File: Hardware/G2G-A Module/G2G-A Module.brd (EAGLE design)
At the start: 13.1 x 12.8 mm, 4 parts, among them J1 GROVE-4P-2.0-3470130P1

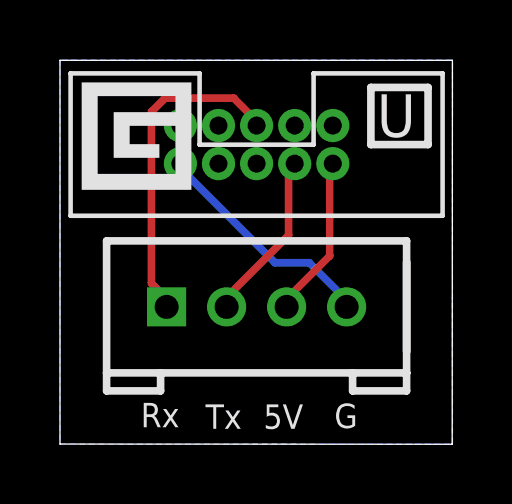
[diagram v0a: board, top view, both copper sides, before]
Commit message: Added G2G-A and G2G-I modules.
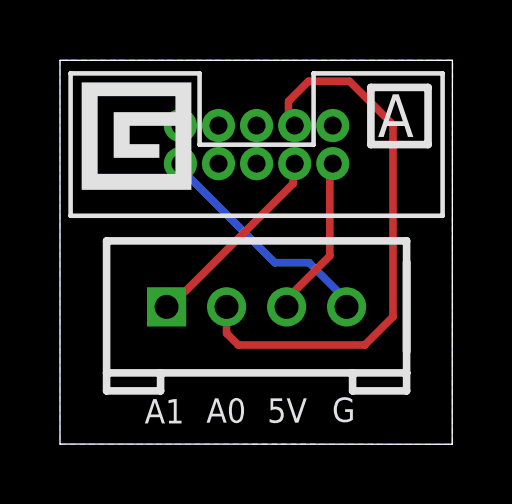
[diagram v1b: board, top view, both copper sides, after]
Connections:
- removed net RX: J1.1, U$1.5
- removed net TX: J1.2, U$1.4
- new net A0: J1.2, U$1.3
- new net A1: J1.1, U$1.4
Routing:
- net A0: track 0.00 -> 18.6 mm
- net RX: track 10.9 -> 0.00 mm
- net A1: track 0.00 -> 6.59 mm
- net TX: track 5.75 -> 0.00 mm
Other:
- board text added: "A"
- board text added: "A0"
- board text added: "A1"
- board text added: "G2G-A"
- board text removed: "G2G-U"
- board text removed: "Rx"
- board text removed: "Tx"
- board text removed: "U"
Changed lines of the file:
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@@
 <wire x1="13.0812" y1="12.7916" x2="0" y2="12.7916" width="0" layer="20"/>
 <wire x1="0" y1="12.7916" x2="0" y2="0" width="0" layer="20"/>
-<text x="10.5664" y="10.2362" size="1.4224" layer="21">U</text>
+<text x="10.5918" y="10.2362" size="1.4224" layer="21">A</text>
 <wire x1="10.3632" y1="11.8872" x2="10.3632" y2="9.9822" width="0.254" layer="21"/>
 <wire x1="10.3632" y1="9.9822" x2="12.2682" y2="9.9822" width="0.254" layer="21"/>
 <wire x1="12.2682" y1="9.9822" x2="12.2682" y2="11.8872" width="0.254" layer="21"/>
 <wire x1="12.2682" y1="11.8872" x2="10.3632" y2="11.8872" width="0.254" layer="21"/>
-<text x="12.5476" y="1.905" size="1.016" layer="22" rot="MR0">G2G-U</text>
+<text x="12.5222" y="1.905" size="1.016" layer="22" rot="MR0">G2G-A</text>
 <text x="12.5222" y="0.6096" size="1.016" layer="22" rot="MR0">v1.0</text>
-<text x="2.6924" y="0.5588" size="0.8128" layer="21">Rx</text>
-<text x="4.8514" y="0.508" size="0.8128" layer="21">Tx</text>
-<text x="6.7818" y="0.508" size="0.8128" layer="21">5V</text>
-<text x="9.144" y="0.5334" size="0.8128" layer="21">G</text>
-<text x="12.5984" y="5.7912" size="1.4224" layer="22" rot="MR0">Gadgeteer.in'</text>
+<text x="6.9088" y="0.7112" size="0.8128" layer="21">5V</text>
+<text x="9.0678" y="0.7366" size="0.8128" layer="21">G</text>
+<text x="12.6238" y="5.7658" size="1.4224" layer="22" rot="MR0">Gadgeteer.in'</text>
 <rectangle x1="0.7225" y1="8.4731" x2="4.3801" y2="8.5493" layer="21"/>
 <rectangle x1="0.7225" y1="8.5493" x2="4.3801" y2="8.6255" layer="21"/>
@@
 <rectangle x1="0.7225" y1="11.9021" x2="4.3801" y2="11.9783" layer="21"/>
 <rectangle x1="0.7225" y1="11.9783" x2="4.3801" y2="12.0545" layer="21"/>
+<text x="4.8768" y="0.7112" size="0.8128" layer="21">A0</text>
+<text x="2.8194" y="0.6858" size="0.8128" layer="21">A1</text>
 </plain>
 <attributes>
@@
 </elements>
 <signals>
-<signal name="TX">
-<contactref element="U$1" pad="4"/>
-<contactref element="J1" pad="2"/>
-<wire x1="7.62" y1="6.9596" x2="7.62" y2="9.2456" width="0.254" layer="1"/>
-<wire x1="5.5626" y1="4.9022" x2="7.62" y2="6.9596" width="0.254" layer="1"/>
-<wire x1="7.62" y1="9.2456" x2="7.8232" y2="9.3472" width="0.254" layer="1"/>
-<wire x1="5.5626" y1="4.9022" x2="5.5532" y2="4.572" width="0.254" layer="1"/>
-</signal>
-<signal name="RX">
-<contactref element="U$1" pad="5"/>
-<contactref element="J1" pad="1"/>
-<wire x1="6.477" y1="10.8458" x2="6.477" y2="10.6172" width="0.254" layer="1"/>
-<wire x1="5.7912" y1="11.5316" x2="6.477" y2="10.8458" width="0.254" layer="1"/>
-<wire x1="3.5052" y1="11.5316" x2="5.7912" y2="11.5316" width="0.254" layer="1"/>
-<wire x1="3.048" y1="11.0744" x2="3.5052" y2="11.5316" width="0.254" layer="1"/>
-<wire x1="3.048" y1="5.3594" x2="3.048" y2="11.0744" width="0.254" layer="1"/>
-<wire x1="3.5052" y1="4.9022" x2="3.048" y2="5.3594" width="0.254" layer="1"/>
-<wire x1="6.477" y1="10.6172" x2="6.5532" y2="10.6172" width="0.254" layer="1"/>
-<wire x1="3.5052" y1="4.9022" x2="3.5532" y2="4.572" width="0.254" layer="1"/>
-</signal>
 <signal name="GND">
 <contactref element="U$1" pad="10"/>
@@
 <wire x1="7.62" y1="4.9022" x2="7.5532" y2="4.572" width="0.254" layer="1"/>
 </signal>
+<signal name="A0">
+<contactref element="J1" pad="2"/>
+<contactref element="U$1" pad="3"/>
+<wire x1="5.5532" y1="4.572" x2="5.5532" y2="3.6924" width="0.254" layer="1"/>
+<wire x1="5.5532" y1="3.6924" x2="5.9436" y2="3.302" width="0.254" layer="1"/>
+<wire x1="5.9436" y1="3.302" x2="10.16" y2="3.302" width="0.254" layer="1"/>
+<wire x1="10.16" y1="3.302" x2="11.0998" y2="4.2418" width="0.254" layer="1"/>
+<wire x1="11.0998" y1="4.2418" x2="11.0998" y2="10.6426" width="0.254" layer="1"/>
+<wire x1="11.0998" y1="10.6426" x2="9.652" y2="12.0904" width="0.254" layer="1"/>
+<wire x1="9.652" y1="12.0904" x2="8.2804" y2="12.0904" width="0.254" layer="1"/>
+<wire x1="8.2804" y1="12.0904" x2="7.62" y2="11.43" width="0.254" layer="1"/>
+<wire x1="7.62" y1="11.43" x2="7.62" y2="10.8204" width="0.254" layer="1"/>
+<wire x1="7.62" y1="10.8204" x2="7.8232" y2="10.6172" width="0.254" layer="1"/>
+</signal>
+<signal name="A1">
+<contactref element="J1" pad="1"/>
+<contactref element="U$1" pad="4"/>
+<wire x1="7.7724" y1="8.6868" x2="7.7724" y2="9.144" width="0.254" layer="1"/>
+<wire x1="3.6576" y1="4.572" x2="7.7724" y2="8.6868" width="0.254" layer="1"/>
+<wire x1="7.7724" y1="9.144" x2="7.8232" y2="9.3472" width="0.254" layer="1"/>
+<wire x1="3.6576" y1="4.572" x2="3.5532" y2="4.572" width="0.254" layer="1"/>
+</signal>
 </signals>
